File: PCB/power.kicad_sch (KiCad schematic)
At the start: 18 parts

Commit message: New version with FTDI chip instead of STM32 and ICE40HX FPGA instead of slower ones
Signed-off-by: Alexis Jeandet <alexis.jeandet@member.fsf.org>
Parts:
- C801, C802, C803, C804, C805: value (none) -> 10uF; footprint (none) -> Capacitor_SMD:C_1206_3216Metric_Pad1.42x1.75mm_HandSolder
- C806: value (none) -> 100nF; footprint (none) -> Capacitor_SMD:C_0402_1005Metric
- C807, C808, C809, C810: value (none) -> 22uF; footprint (none) -> Capacitor_SMD:C_1206_3216Metric_Pad1.42x1.75mm_HandSolder
- L801, L802: value (none) -> 2.2uH; footprint (none) -> Inductor_SMD:L_1206_3216Metric_Pad1.42x1.75mm_HandSolder
- L803: value (none) -> 1uH; footprint (none) -> Inductor_SMD:L_1206_3216Metric_Pad1.42x1.75mm_HandSolder
- R801: value (none) -> 1M; footprint (none) -> Resistor_SMD:R_0603_1608Metric_Pad1.05x0.95mm_HandSolder
- R802: value (none) -> 91k; footprint (none) -> Resistor_SMD:R_0603_1608Metric_Pad1.05x0.95mm_HandSolder
- U801: value (none) -> tps6240x; footprint (none) -> Package_SON:Texas_S-PVSON-N10_ThermalVias
- U802: value (none) -> TPS63060; footprint (none) -> Package_SON:Texas_S-PWSON-N10_ThermalVias
- U803: value (none) -> NCP718xSN500; footprint (none) -> Package_TO_SOT_SMD:SOT-23-5

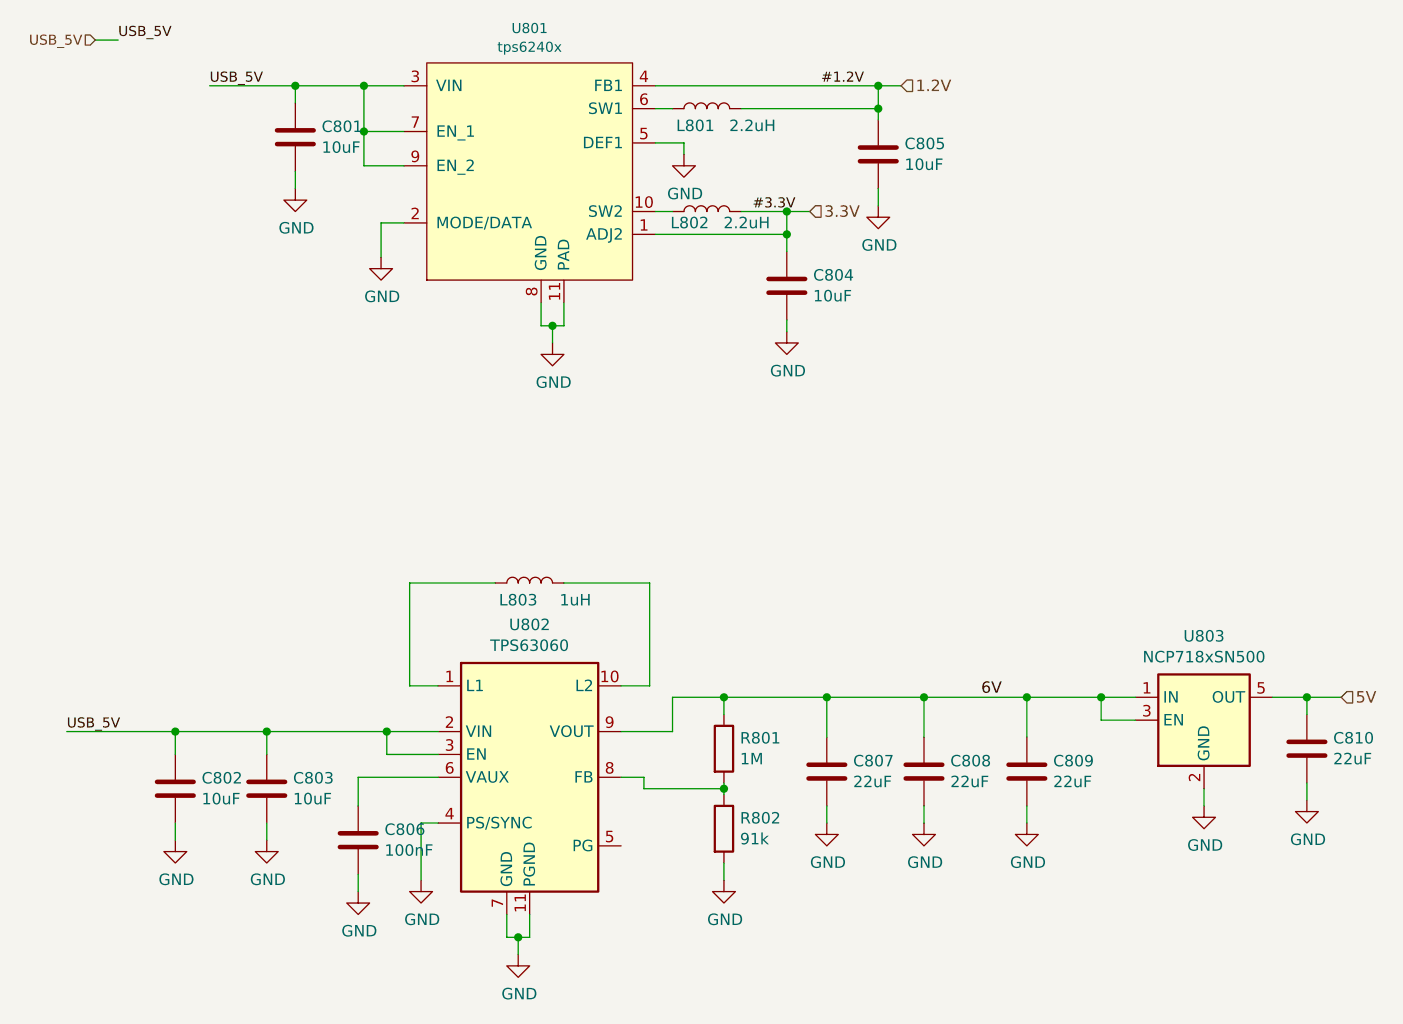
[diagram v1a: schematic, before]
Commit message: adds UGA and few sch libs update
Signed-off-by: Alexis Jeandet <alexis.jeandet@member.fsf.org>
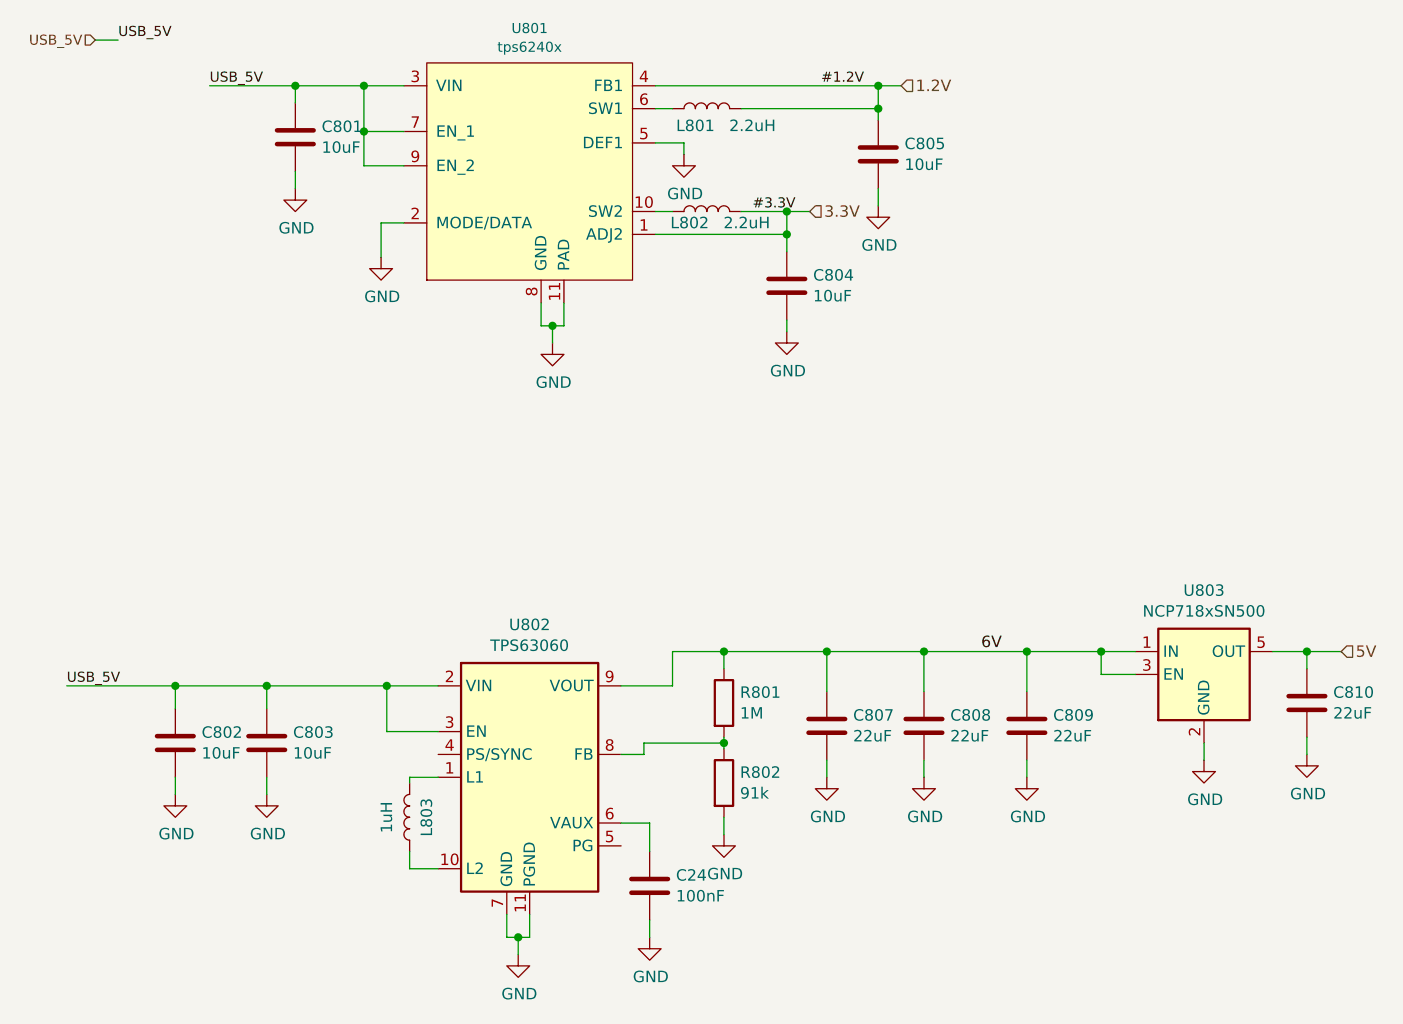
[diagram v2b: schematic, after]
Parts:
- removed C806: 100nF, Capacitor_SMD:C_0402_1005Metric, symbol Device:C
- added C24: 100nF, Capacitor_SMD:C_0402_1005Metric, symbol Device:C
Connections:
- net GND: now also C24.2; no longer U802.4 (PS/SYNC)
- net at U802.6 (VAUX): now also C24.1
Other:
- moved on the sheet: C802, C803, C807, C808, C809, C810, L803, R801, R802, U803
